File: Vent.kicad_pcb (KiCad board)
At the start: 4 copper layers, 38.1 x 17.6 mm, 26 parts, among them J2 B2B-XH-A_LF__SN_, J3 Conn_01x03_Pin, J4 Conn_01x04_Socket, SW1 SW_Push, U1 ESP32-H2-MINI-1-H2, U4 MCP1640x-xMC

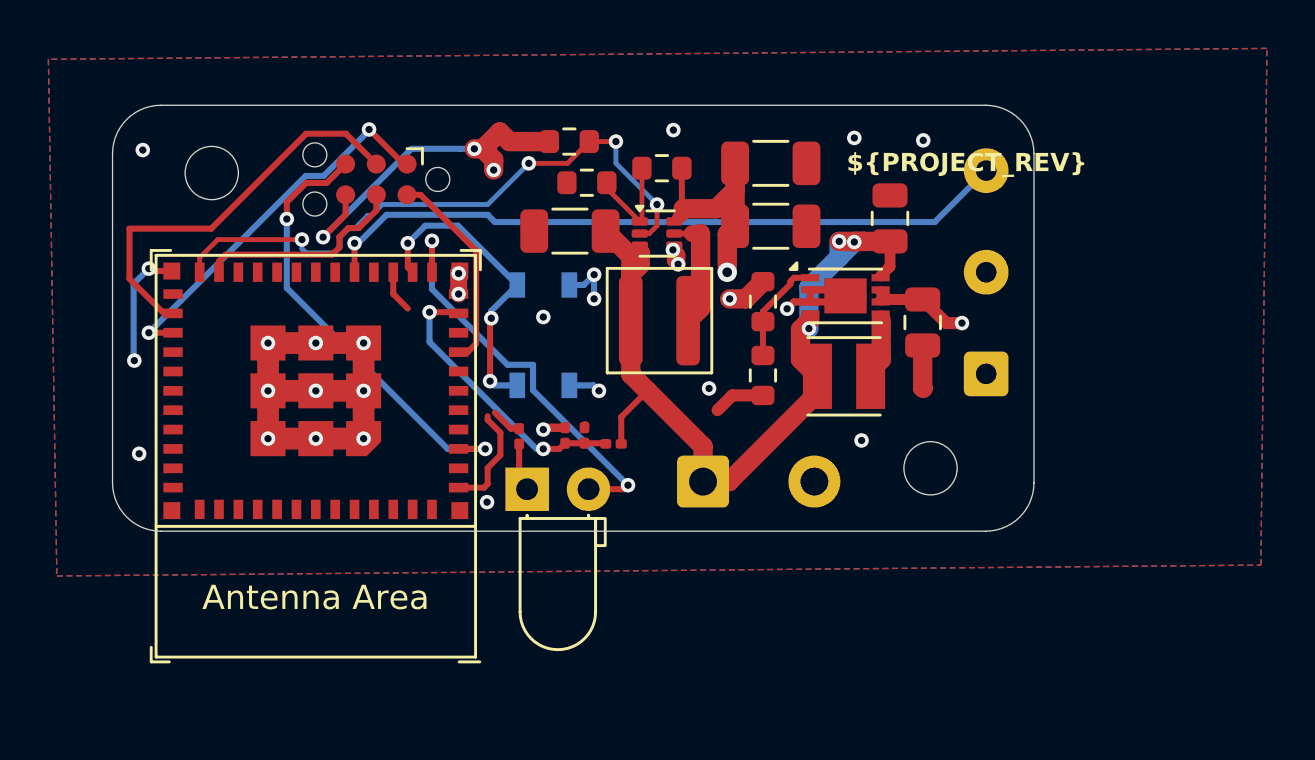
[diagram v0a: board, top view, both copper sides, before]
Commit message: feat: Change the ESP32 H2 symbol to be from PCM_Espressif
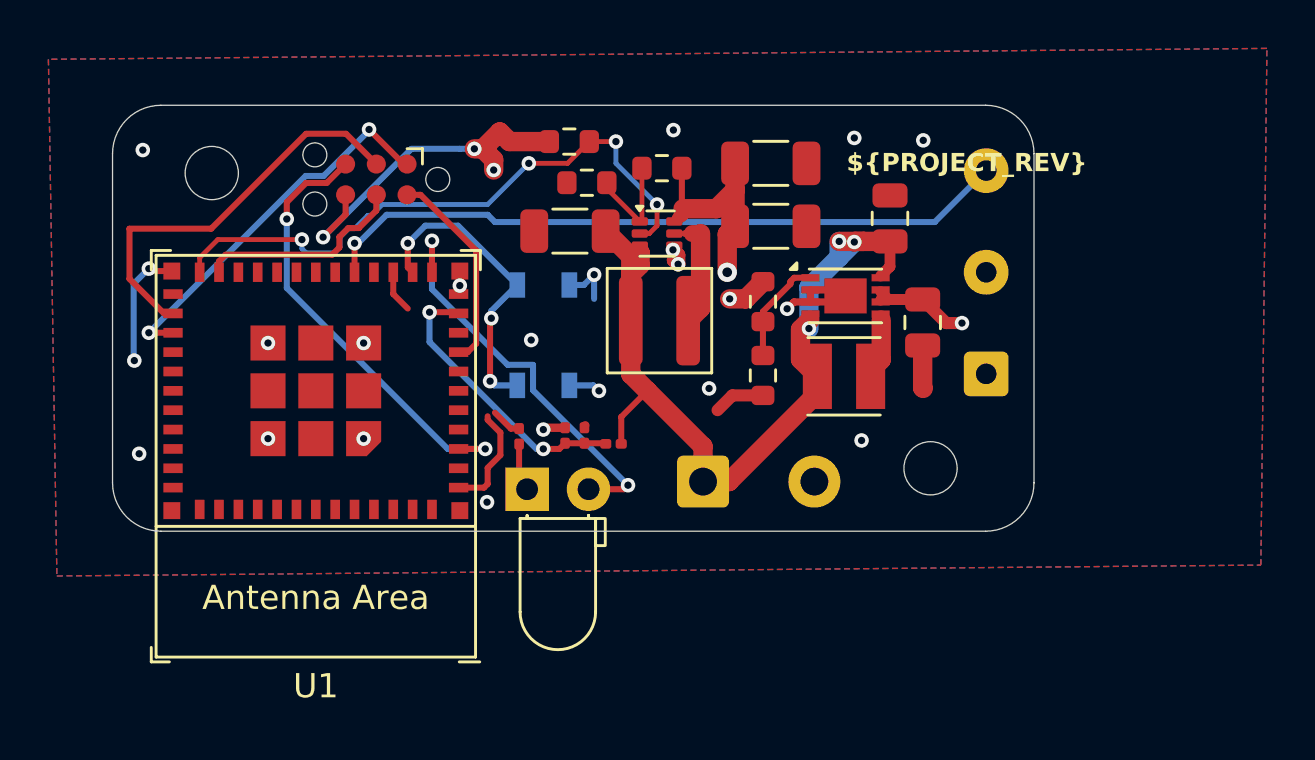
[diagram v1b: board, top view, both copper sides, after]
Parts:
- U1: value ESP32-H2-MINI-1-H2 -> ESP32-H2-MINI-1
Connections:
- J4 pad 1: /IO27 -> /RXD0
- J4 pad 3: /IO26 -> /TXD0
- U1 pad 18: /IO4 -> unconnected-(U1-GPIO4/FSPICLK/ADC1_CH3/MTCK-Pad18)
- U1 pad 19: /IO5 -> unconnected-(U1-GPIO5/FSPID/ADC1_CH4/MTDI-Pad19)
- U1 pad 20: /IO10 -> unconnected-(U1-GPIO10/ZCD0-Pad20)
- U1 pad 21: /IO11 -> unconnected-(U1-GPIO11/ZCD1-Pad21)
- U1 pad 26: /IO26 -> /TXD0
- U1 pad 27: /IO27 -> /RXD0
- U1 pad 30: /RXD0 -> unconnected-(U1-GPIO23/FSPICS1/U0RXD-Pad30)
- U1 pad 31: /TXD0 -> unconnected-(U1-GPIO24/FSPICS2/U0TXD-Pad31)
- U1 pad 5: /IO2 -> unconnected-(U1-GPIO2/FSPIWP/ADC1_CH1/MTMS-Pad5)
- U1 pad 6: /IO3 -> unconnected-(U1-GPIO3/FSPIHD/ADC1_CH2/MTDO-Pad6)
- U1 pad 9: /IO0 -> unconnected-(U1-GPIO0/FSPIQ-Pad9)
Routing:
- net GND: track 62.9 -> 43.1 mm, vias 32 -> 25
- net /TXD0: track 0.00 -> 16.8 mm
- net /IO26: track 16.8 -> 0.00 mm
- net /RXD0: track 0.00 -> 15.8 mm, vias 0 -> 2
- net /IO27: track 15.8 -> 0.00 mm, vias 2 -> 0

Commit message: replace tx0 and rx0 with D+ and D-
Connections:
- net /RXD0 renamed /D+
- net /TXD0 renamed /D-
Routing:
- net /D-: track 16.8 -> 13.4 mm
- net /D+: track 15.8 -> 14.5 mm, vias 2 -> 0
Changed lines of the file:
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@@
 				(name "A")
 				(pins "8" "10" "12" "13" "24" "25" "17" "28" "29" "32" "33" "34" "35"
-					"4" "7" "3" "48" "1" "2" "49" "50" "11" "14" "51" "52" "53" "47" "36"
-					"37" "38" "39" "40" "41" "42" "43" "44" "45" "46" "15" "9" "31" "30"
+					"4" "7" "3" "53" "38" "44" "11" "2" "1" "14" "43" "52" "51" "42" "50"
+					"49" "48" "47" "46" "41" "40" "39" "36" "37" "45" "15" "9" "31" "30"
 					"27" "26" "5" "6" "18" "19" "20" "21" "22" "23" "16"
 				)
@@
 			(size 0.4 0.8)
 			(layers "F.Cu" "F.Mask" "F.Paste")
-			(net "/TXD0")
+			(net "/D-")
 			(pinfunction "GPIO26/FSPICS4/USB_D-_26")
 			(pintype "bidirectional")
@@
 			(size 0.4 0.8)
 			(layers "F.Cu" "F.Mask" "F.Paste")
-			(net "/RXD0")
+			(net "/D+")
 			(pinfunction "GPIO27/FSPICS5/USB_D+_27")
 			(pintype "bidirectional")
@@
 			(size 0.7874 0.7874)
 			(layers "F.Cu" "F.Mask")
-			(net "/RXD0")
+			(net "/D+")
 			(pinfunction "RX_1")
 			(pintype "bidirectional")
@@
 			(size 0.7874 0.7874)
 			(layers "F.Cu" "F.Mask")
-			(net "/TXD0")
+			(net "/D-")
 			(pinfunction "TX_3")
 			(pintype "bidirectional")
@@
 	)
 	(via
-		(at 128.625 73.575)
-		(size 0.6)
-		(drill 0.3)
-		(layers "F.Cu" "B.Cu")
-		(net "GND")
-	)
-	(via
 		(at 130.9 65.25)
 		(size 0.6)
@@
 	)
 	(via
-		(at 132.575 73.575)
-		(size 0.6)
-		(drill 0.3)
-		(layers "F.Cu" "B.Cu")
-		(net "GND")
-	)
-	(via
 		(at 136.55 67.25)
 		(size 0.6)
@@
 	)
 	(via
-		(at 128.625 69.625)
-		(size 0.6)
-		(drill 0.3)
-		(layers "F.Cu" "B.Cu")
-		(net "GND")
-	)
-	(via
 		(at 140 73.2)
 		(size 0.6)
@@
 	)
 	(via
+		(at 126.6 73.6)
+		(size 0.6)
+		(drill 0.3)
+		(layers "F.Cu" "B.Cu")
+		(free yes)
+		(net "GND")
+	)
+	(via
 		(at 150.075001 68.208883)
 		(size 0.6)
@@
 	)
 	(via
-		(at 132.575 69.625)
+		(at 126.4 68.4)
 		(size 0.6)
 		(drill 0.3)
 		(layers "F.Cu" "B.Cu")
+		(free yes)
 		(net "GND")
 	)
@@
 	)
 	(via
+		(at 134.4 74.2)
+		(size 0.6)
+		(drill 0.3)
+		(layers "F.Cu" "B.Cu")
+		(free yes)
+		(net "GND")
+	)
+	(via
 		(at 139.5 69.5)
 		(size 0.6)
@@
 		(net "GND")
 	)
+	(via
+		(at 134.2 69.6)
+		(size 0.6)
+		(drill 0.3)
+		(layers "F.Cu" "B.Cu")
+		(free yes)
+		(net "GND")
+	)
 	(segment
 		(start 142.075 71.375)
@@
 	)
 	(segment
-		(start 122.9 66.974)
-		(end 124.326 68.4)
-		(width 0.25)
-		(layer "F.Cu")
-		(net "/TXD0")
-	)
-	(segment
-		(start 131.8477 60.9777)
-		(end 130.199096 60.9777)
-		(width 0.25)
-		(layer "F.Cu")
-		(net "/TXD0")
-	)
-	(segment
-		(start 133.1 62.23)
-		(end 131.8477 60.9777)
-		(width 0.25)
-		(layer "F.Cu")
-		(net "/TXD0")
-	)
-	(segment
-		(start 124.326 68.4)
-		(end 124.7 68.4)
-		(width 0.25)
-		(layer "F.Cu")
-		(net "/TXD0")
-	)
-	(segment
-		(start 126.276796 64.9)
-		(end 122.9 64.9)
-		(width 0.25)
-		(layer "F.Cu")
-		(net "/TXD0")
-	)
-	(segment
-		(start 122.9 64.9)
-		(end 122.9 66.974)
-		(width 0.25)
-		(layer "F.Cu")
-		(net "/TXD0")
-	)
-	(segment
-		(start 130.199096 60.9777)
-		(end 126.276796 64.9)
-		(width 0.25)
-		(layer "F.Cu")
-		(net "/TXD0")
-	)
-	(segment
-		(start 123.7 69.2)
-		(end 124.7 69.2)
-		(width 0.25)
-		(layer "F.Cu")
-		(net "/RXD0")
-	)
-	(segment
-		(start 134.23 62.23)
-		(end 132.8 60.8)
-		(width 0.25)
-		(layer "F.Cu")
-		(net "/RXD0")
-	)
-	(segment
-		(start 134.37 62.23)
-		(end 134.23 62.23)
-		(width 0.25)
-		(layer "F.Cu")
-		(net "/RXD0")
-	)
-	(via
-		(at 132.8 60.8)
-		(size 0.6)
-		(drill 0.3)
-		(layers "F.Cu" "B.Cu")
-		(capping no)
-		(covering
-			(front no)
-			(back no)
-		)
-		(plugging
-			(front no)
-			(back no)
-		)
-		(filling no)
-		(net "/RXD0")
-	)
-	(via
-		(at 123.7 69.2)
-		(size 0.6)
-		(drill 0.3)
-		(layers "F.Cu" "B.Cu")
-		(capping no)
-		(covering
-			(front no)
-			(back no)
-		)
-		(plugging
-			(front no)
-			(back no)
-		)
-		(filling no)
-		(net "/RXD0")
-	)
-	(segment
-		(start 132.8 60.841204)
-		(end 130.920904 62.7203)
-		(width 0.25)
-		(layer "B.Cu")
-		(net "/RXD0")
-	)
-	(segment
-		(start 130.920904 62.7203)
-		(end 130.1797 62.7203)
-		(width 0.25)
-		(layer "B.Cu")
-		(net "/RXD0")
-	)
-	(segment
-		(start 132.8 60.8)
-		(end 132.8 60.841204)
-		(width 0.25)
-		(layer "B.Cu")
-		(net "/RXD0")
-	)
-	(segment
-		(start 130.1797 62.7203)
-		(end 123.7 69.2)
-		(width 0.25)
-		(layer "B.Cu")
-		(net "/RXD0")
-	)
-	(segment
 		(start 139 73.8)
 		(end 139 75.335)
@@
 		(net "Net-(U2-SW)")
 	)
+	(segment
+		(start 132.6 67.3)
+		(end 126.7 67.3)
+		(width 0.2)
+		(layer "F.Cu")
+		(net "/D+")
+	)
+	(segment
+		(start 132.6 66.1)
+		(end 132.6 67.3)
+		(width 0.2)
+		(layer "F.Cu")
+		(net "/D+")
+	)
+	(segment
+		(start 133.6937 65.0063)
+		(end 132.6 66.1)
+		(width 0.2)
+		(layer "F.Cu")
+		(net "/D+")
+	)
+	(segment
+		(start 126.7 67.3)
+		(end 124.8 69.2)
+		(width 0.2)
+		(layer "F.Cu")
+		(net "/D+")
+	)
+	(segment
+		(start 134.37 62.23)
+		(end 133.6937 62.9063)
+		(width 0.2)
+		(layer "F.Cu")
+		(net "/D+")
+	)
+	(segment
+		(start 133.6937 62.9063)
+		(end 133.6937 65.0063)
+		(width 0.2)
+		(layer "F.Cu")
+		(net "/D+")
+	)
+	(segment
+		(start 124.8 69.2)
+		(end 124.7 69.2)
+		(width 0.2)
+		(layer "F.Cu")
+		(net "/D+")
+	)
+	(segment
+		(start 130.209865 61.0037)
+		(end 125.4 65.813565)
+		(width 0.2)
+		(layer "F.Cu")
+		(net "/D-")
+	)
+	(segment
+		(start 125 68.4)
+		(end 124.7 68.4)
+		(width 0.2)
+		(layer "F.Cu")
+		(net "/D-")
+	)
+	(segment
+		(start 133.1 62.23)
+		(end 131.8737 61.0037)
+		(width 0.2)
+		(layer "F.Cu")
+		(net "/D-")
+	)
+	(segment
+		(start 125.4 65.813565)
+		(end 125.4 68)
+		(width 0.2)
+		(layer "F.Cu")
+		(net "/D-")
+	)
+	(segment
+		(start 133.03 62.23)
+		(end 133 62.2)
+		(width 0.2)
+		(layer "F.Cu")
+		(net "/D-")
+	)
+	(segment
+		(start 125.4 68)
+		(end 125 68.4)
+		(width 0.2)
+		(layer "F.Cu")
+		(net "/D-")
+	)
+	(segment
+		(start 133.1 62.23)
+		(end 133.03 62.23)
+		(width 0.2)
+		(layer "F.Cu")
+		(net "/D-")
+	)
+	(segment
+		(start 131.8737 61.0037)
+		(end 130.209865 61.0037)
+		(width 0.2)
+		(layer "F.Cu")
+		(net "/D-")
+	)
 	(zone
 		(net "GND")
@@
 	)
 	(group ""
-		(members "4aa62e9d-fe5b-45dd-a4c4-f0f6c7ce18a0")
-	)
-	(group ""
-		(members "a3147304-401d-4d50-8d6f-409a5df0fde4")
-	)
-	(group ""
